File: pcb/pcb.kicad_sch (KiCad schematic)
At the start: 88 parts, among them J1 TRRS, J2 TRRS, SW1 SW_PUSH, SW10 SW_PUSH, SW11 SW_PUSH, SW12 SW_PUSH, SW13 SW_PUSH, SW14 SW_PUSH, SW15 SW_PUSH, SW16 SW_PUSH, SW17 SW_PUSH, SW18 SW_PUSH, SW19 SW_PUSH, SW2 SW_PUSH, SW20 SW_PUSH, SW21 SW_PUSH, SW22 SW_PUSH, SW23 SW_PUSH, SW24 SW_PUSH, SW25 SW_PUSH, SW26 SW_PUSH, SW27 SW_PUSH, SW28 SW_PUSH, SW29 SW_PUSH, SW3 SW_PUSH, SW30 SW_PUSH, SW31 SW_PUSH, SW32 SW_PUSH, SW33 SW_PUSH, SW34 SW_PUSH, SW35 SW_PUSH, SW36 SW_PUSH, SW37 SW_PUSH, SW38 SW_PUSH, SW39 SW_PUSH, SW4 SW_PUSH, SW40 SW_PUSH, SW41 SW_PUSH, SW42 SW_PUSH, SW5 SW_PUSH, SW6 SW_PUSH, SW7 SW_PUSH, SW8 SW_PUSH, SW9 SW_PUSH, U1 rp2040-zero, U2 rp2040-zero

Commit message: 1.1: create garbar files, 2.0: create left pcb
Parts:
- D1, D10, D11, D12, D13, D14, D15, D16, D17, D18, D19, D2, D20, D21, D22, D23, D24, D25, D26, D27, D28, D29, D3, D30, D31, D32, D33, D34, D35, D36, D37, D38, D39, D4, D40, D41, D42, D5, D6, D7, D8, D9: footprint kbd:D3_SMD_v2 -> kbd:D3_TH_SMD_v2
- J1, J2: symbol BrownSugar_KBD:TRRS -> kbd:MJ-4PP-9
- SW1, SW27: footprint kbd:ChocV1_V2_Hotswap_1.5u -> kbd:keyswitch_cherrymx_choc12_hotswap_1.5u
- SW10, SW11, SW12, SW14, SW15, SW16, SW17, SW18, SW2, SW20, SW22, SW23, SW24, SW25, SW26, SW28, SW29, SW3, SW30, SW31, SW32, SW33, SW34, SW35, SW36, SW37, SW38, SW4, SW41, SW5, SW6, SW8, SW9: footprint kbd:ChocV1_V2_Hotswap -> kbd:keyswitch_cherrymx_choc12_hotswap_1u
- SW13, SW19, SW21, SW39, SW40, SW42, SW7: footprint kbd:ChocV1_V2_Hotswap_1.25u -> kbd:keyswitch_cherrymx_choc12_hotswap_1.25u
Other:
- moved on the sheet: U1

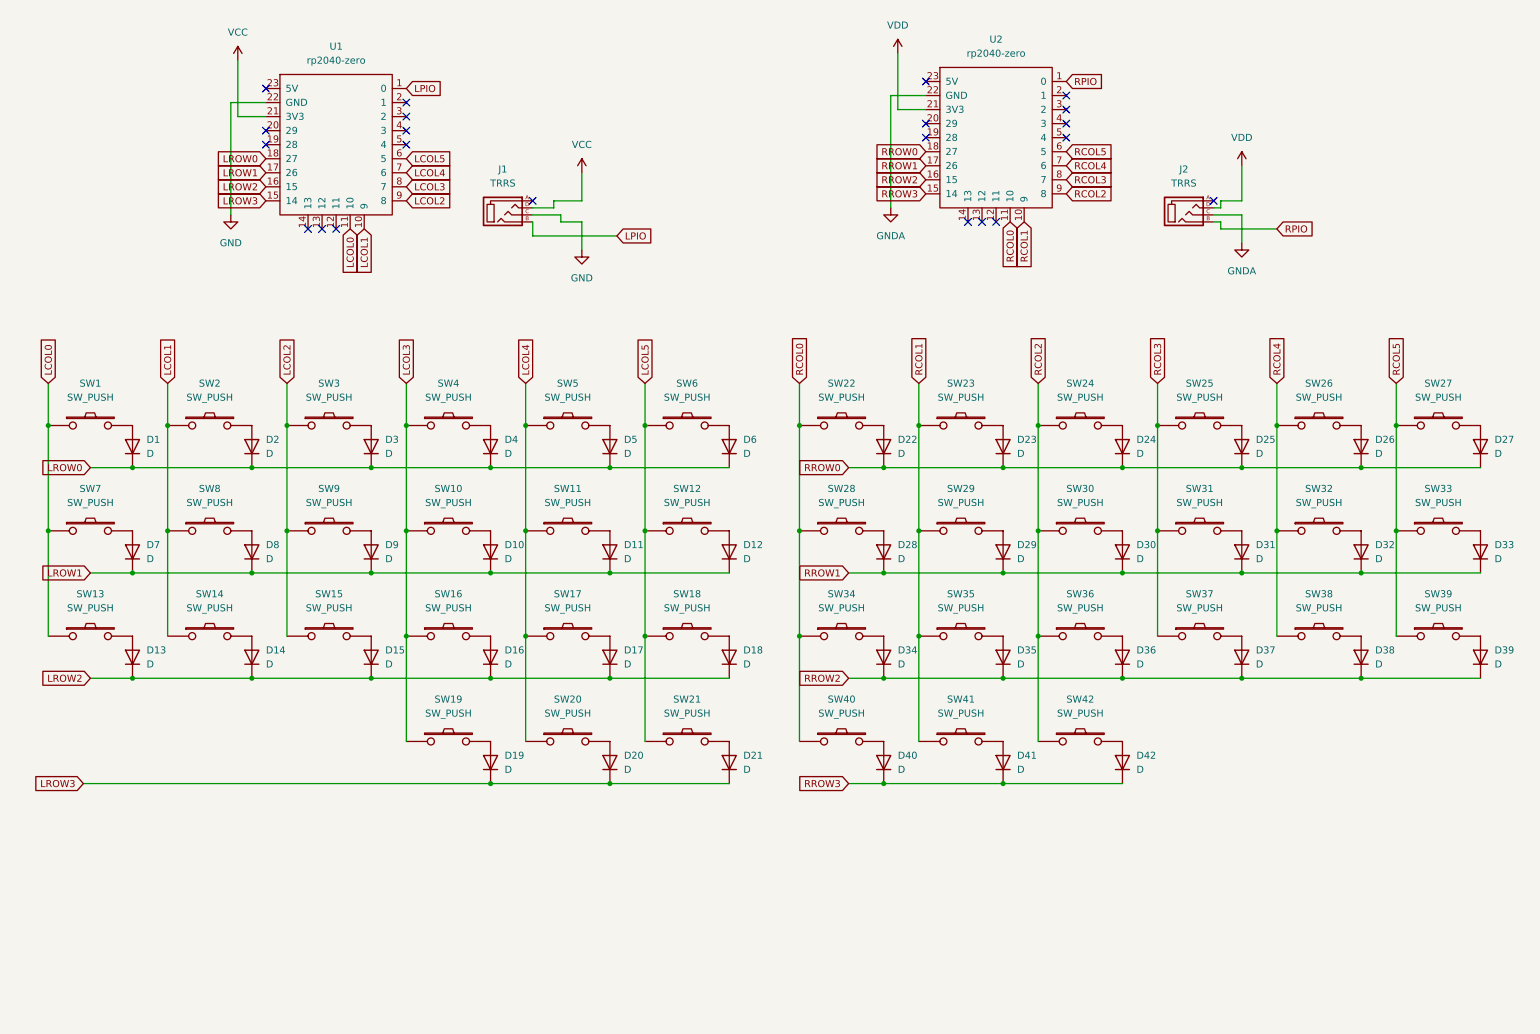
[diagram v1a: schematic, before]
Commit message: refactor: change folder name, old data is no maggie42cs0
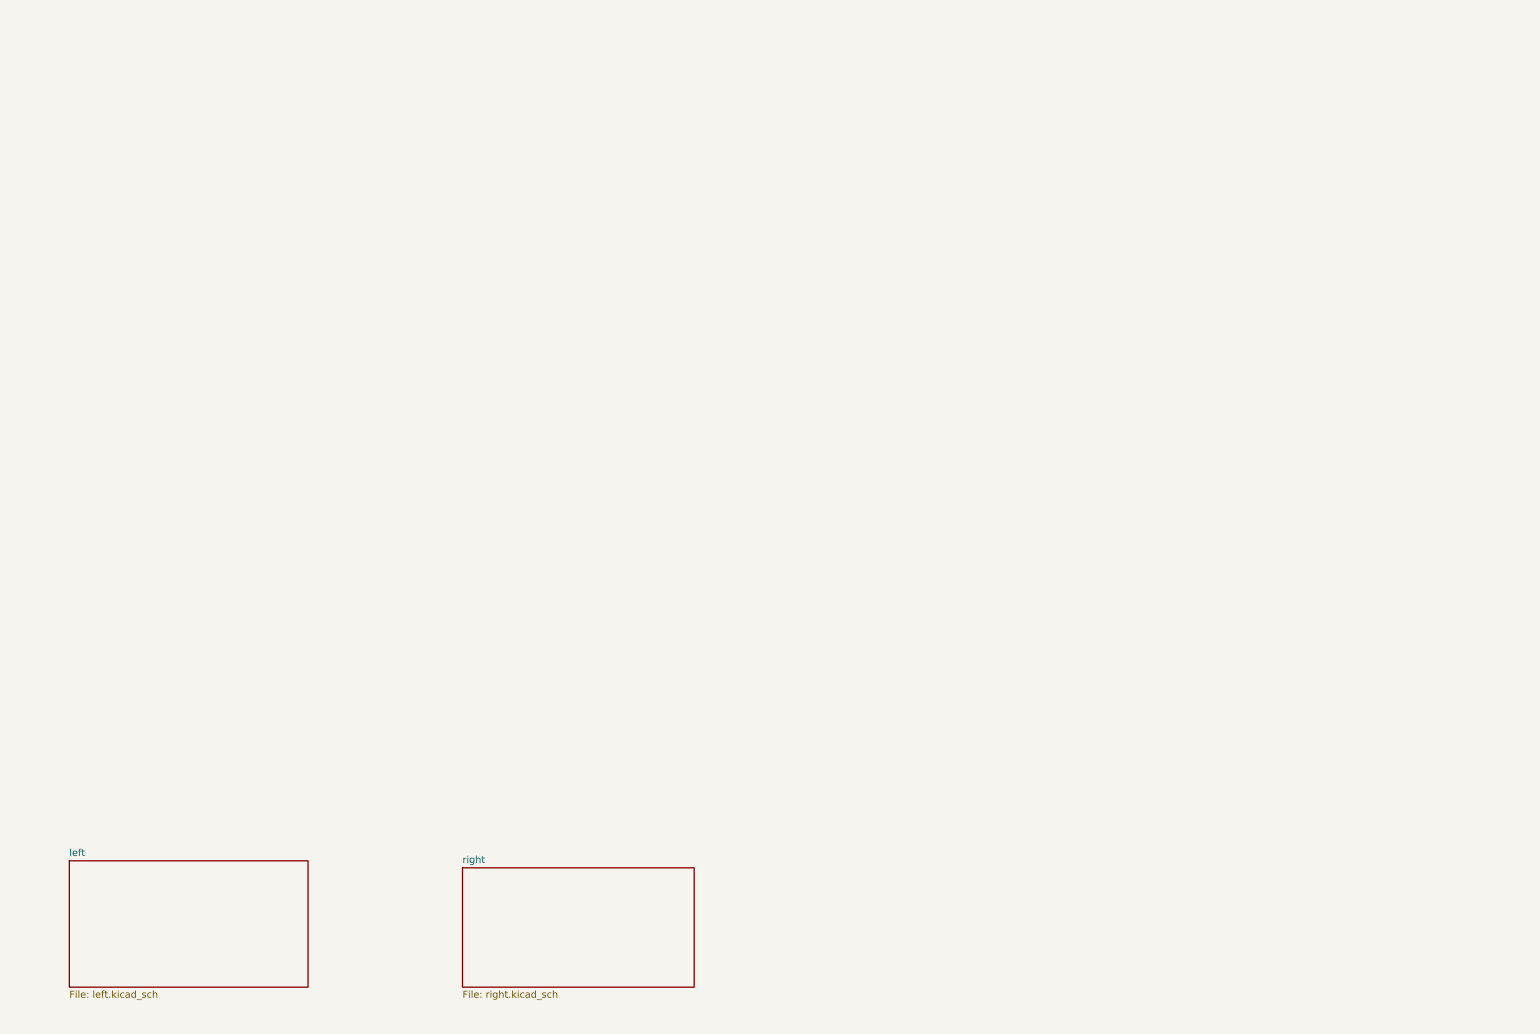
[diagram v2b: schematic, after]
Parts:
- removed D1, D10, D11, D12, D13, D14, D15, D16, D17, D18, D19, D2, D20, D21, D22, D23, D24, D25, D26, D27, D28, D29, D3, D30, D31, D32, D33, D34, D35, D36, D37, D38, D39, D4, D40, D41, D42, D5, D6, D7, D8, D9: D, kbd:D3_TH_SMD_v2, symbol Device:D
- removed J1, J2: TRRS, kbd:MJ-4PP-9_1side, symbol kbd:MJ-4PP-9
- removed SW1, SW27: SW_PUSH, kbd:keyswitch_cherrymx_choc12_hotswap_1.5u, symbol BrownSugar_KBD:SW_PUSH
- removed SW10, SW11, SW12, SW14, SW15, SW16, SW17, SW18, SW2, SW20, SW22, SW23, SW24, SW25, SW26, SW28, SW29, SW3, SW30, SW31, SW32, SW33, SW34, SW35, SW36, SW37, SW38, SW4, SW41, SW5, SW6, SW8, SW9: SW_PUSH, kbd:keyswitch_cherrymx_choc12_hotswap_1u, symbol BrownSugar_KBD:SW_PUSH
- removed SW13, SW19, SW21, SW39, SW40, SW42, SW7: SW_PUSH, kbd:keyswitch_cherrymx_choc12_hotswap_1.25u, symbol BrownSugar_KBD:SW_PUSH
- removed U1, U2: rp2040-zero, mcu:rp2040-zero-tht, symbol mcu:rp2040-zero
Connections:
- no-connect marks 22 -> 0
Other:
- added sheet left (left.kicad_sch)
- added sheet right (right.kicad_sch)
- title: (none) -> maggie42cs

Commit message: wip: layout
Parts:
- added C1, C16, C17, C2: 10u, Capacitor_SMD:C_0402_1005Metric, symbol Device:C_Small
- added C10, C11, C12, C13, C18, C19, C20, C23, C24, C25, C26, C27, C28, C3, C31, C33, C4, C7, C8, C9: 100n, Capacitor_SMD:C_0402_1005Metric, symbol Device:C_Small
- added C14, C15, C29, C30: 30pF, Capacitor_SMD:C_0603_1608Metric, symbol Device:C_Small
- added C21, C22, C32, C34, C5, C6: 2.2uF, Capacitor_SMD:C_0402_1005Metric, symbol Device:C_Small
- added F1, F2: ~, Fuse:Fuse_0603_1608Metric, symbol Device:Polyfuse_Small
- added J1, J4: AudioJack3, kbd:PJ-399B-6A_margin, symbol Connector_Audio:AudioJack3
- added J2, J5: USB_C_Receptacle_USB2.0_16P, Connector_USB:USB_C_Receptacle_HRO_TYPE-C-31-M-12, symbol Connector:USB_C_Receptacle_USB2.0_16P
- added J3, J6: Conn_01x03_Pin, Connector_PinHeader_2.54mm:PinHeader_1x03_P2.54mm_Vertical, symbol Connector:Conn_01x03_Pin
- added R1, R10, R2, R9: 5.1k, Resistor_SMD:R_0402_1005Metric, symbol Device:R_Small
- added R11, R4: 5.6k, Resistor_SMD:R_0603_1608Metric, symbol Device:R_Small
- added R12, R16, R18, R20, R3, R8: 1k, Resistor_SMD:R_0402_1005Metric, symbol Device:R_Small
- added R13, R17, R19, R5: 10k, Resistor_SMD:R_0402_1005Metric, symbol Device:R_Small
- added R14, R15, R6, R7: 27, Resistor_SMD:R_0402_1005Metric, symbol Device:R_Small
- added SD1, SD2: ~, Diode_SMD:D_SOD-123, symbol Device:D_Schottky_Small
- added SMDSW1, SMDSW3: RESET, Button_Switch_SMD:SW_Push_1P1T_XKB_TS-1187A, symbol Switch:SW_Push
- added SMDSW2, SMDSW4: BOOT, Button_Switch_SMD:SW_Push_1P1T_XKB_TS-1187A, symbol Switch:SW_Push
- added STLED1, STLED2: WHITE, LED_SMD:LED_0603_1608Metric, symbol Device:LED_Small
- added U1, U4: NCP1117-3.3_SOT223, Package_TO_SOT_SMD:SOT-223-3_TabPin2, symbol Regulator_Linear:NCP1117-3.3_SOT223
- added U2, U5: RP2040, Package_DFN_QFN:QFN-56-1EP_7x7mm_P0.4mm_EP3.2x3.2mm, symbol MCU_RaspberryPi:RP2040
- added U3, U6: W25Q128JVS, Package_SO:SOIC-8_5.23x5.23mm_P1.27mm, symbol Memory_Flash:W25Q128JVS
- added Y1, Y2: 12MHz, Crystal:Crystal_SMD_3225-4Pin_3.2x2.5mm, symbol Device:Crystal_GND24_Small
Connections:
- new net: R15.2, U5.46 (USB_DM)
- new net: C29.2, U5.20 (XIN), Y2.1
- new net: SMDSW1.2, U2.26 (RUN)
- new net: R7.2, U2.46 (USB_DM)
- new net: C30.2, R16.1, Y2.3
- new net: R20.2, SMDSW4.2
- new net: J2.A5 (CC1), R1.1
- new net: J2.B5 (CC2), R2.1
- new net: C14.2, U2.20 (XIN), Y1.1
- new net: C15.2, R8.1, Y1.3
- new net: J5.A5 (CC1), R9.1
- new net: R3.1, STLED1.2 (A)
- new net: F1.2, R4.1, SD1.2 (A)
- new net: R6.2, U2.47 (USB_DP)
- new net: R16.2, U5.21 (XOUT)
- new net: J6.1 (Pin_1), U5.24 (SWCLK)
- new net: J6.3 (Pin_3), U5.25 (SWD)
- new net: SMDSW3.2, U5.26 (RUN)
- new net: R14.2, U5.47 (USB_DP)
- new net: F2.2, R11.1, SD2.2 (A)
- new net: J3.1 (Pin_1), U2.24 (SWCLK)
- new net: J3.3 (Pin_3), U2.25 (SWD)
- new net: J5.B5 (CC2), R10.1
- new net: R18.2, SMDSW2.2
- new net: R8.2, U2.21 (XOUT)
- new net: R12.1, STLED2.2 (A)
- new net +1V1: C3.1, C4.1, C5.1, U2.23 (DVDD), U2.45 (VREG_VOUT), U2.50 (DVDD)
- new net +3V3: C10.1, C11.1, C12.1, C13.1, C2.1, C31.2, C32.2, C6.1, C7.1, C8.1, C9.1, R17.2, R3.2, U1.2 (VO), U2.1 (IOVDD), U2.10 (IOVDD), U2.22 (IOVDD), U2.33 (IOVDD), U2.42 (IOVDD), U2.43 (ADC_AVDD), U2.44 (VREG_IN), U2.48 (USB_VDD), U2.49 (IOVDD), U3.8 (VCC)
- new net +5V: C1.1, J1.T, SD1.1 (K), U1.3 (VI)
- new net COL0: U2.8 (GPIO6)
- new net COL1: U2.9 (GPIO7)
- new net COL2: U2.11 (GPIO8)
- new net COL3: U2.12 (GPIO9)
- new net COL4: U2.13 (GPIO10)
- new net COL5: U2.14 (GPIO11)
- new net CONN: J1.R, U2.2 (GPIO0)
- new net D+: J2.A6 (D+), J2.B6 (D+), R6.1
- new net D-: J2.A7 (D-), J2.B7 (D-), R7.1
- new net GND: C1.2, C10.2, C11.2, C12.2, C13.2, C14.1, C15.1, C2.2, C3.2, C31.1, C32.1, C4.2, C5.2, C6.2, C7.2, C8.2, C9.2, J1.S, J2.A1 (GND), J2.A12 (GND), J2.B1 (GND), J2.B12 (GND), J2.S1 (SHIELD), J3.2 (Pin_2), R1.2, R13.2, R2.2, R5.2, SMDSW1.1, SMDSW2.1, STLED1.1 (K), U1.1 (GND), U2.19 (TESTEN), U2.57 (GND), U3.4 (GND), Y1.2, Y1.4
- new net QSPI_SCLK: U2.52 (QSPI_SCLK), U3.6 (CLK)
- new net QSPI_SD0: U2.53 (QSPI_SD0), U3.5 (DI(IO0))
- new net QSPI_SD1: U2.55 (QSPI_SD1), U3.2 (DO(IO1))
- new net QSPI_SD2: U2.54 (QSPI_SD2), U3.3 (IO2)
- new net QSPI_SD3: U2.51 (QSPI_SD3), U3.7 (IO3)
- new net QSPI_SS: R17.1, R18.1, U2.56 (QSPI_SS), U3.1 (~{CS})
- new net ROW0: U2.4 (GPIO2)
- new net ROW1: U2.5 (GPIO3)
- new net ROW2: U2.6 (GPIO4)
- new net ROW3: U2.7 (GPIO5)
- new net USB: R4.2, R5.1, U2.3 (GPIO1)
- new net VBUS: F1.1, J2.A4 (VBUS), J2.A9 (VBUS), J2.B4 (VBUS), J2.B9 (VBUS)
- new net VBUSR: F2.1, J5.A4 (VBUS), J5.A9 (VBUS), J5.B4 (VBUS), J5.B9 (VBUS)
- new net r+1V1: C18.1, C19.1, C21.1, U5.23 (DVDD), U5.45 (VREG_VOUT), U5.50 (DVDD)
- new net r+3V3: C17.1, C20.1, C22.1, C23.1, C24.1, C25.1, C26.1, C27.1, C28.1, C33.2, C34.2, R12.2, R19.2, U4.2 (VO), U5.1 (IOVDD), U5.10 (IOVDD), U5.22 (IOVDD), U5.33 (IOVDD), U5.42 (IOVDD), U5.43 (ADC_AVDD), U5.44 (VREG_IN), U5.48 (USB_VDD), U5.49 (IOVDD), U6.8 (VCC)
- new net r+5V: C16.1, J4.T, SD2.1 (K), U4.3 (VI)
- new net rCOL0: U5.8 (GPIO6)
- new net rCOL1: U5.9 (GPIO7)
- new net rCOL2: U5.11 (GPIO8)
- new net rCOL3: U5.12 (GPIO9)
- new net rCOL4: U5.13 (GPIO10)
- new net rCOL5: U5.14 (GPIO11)
- new net rCONN: J4.R, U5.2 (GPIO0)
- new net rD+: J5.A6 (D+), J5.B6 (D+), R14.1
- new net rD-: J5.A7 (D-), J5.B7 (D-), R15.1
- new net rGND: C16.2, C17.2, C18.2, C19.2, C20.2, C21.2, C22.2, C23.2, C24.2, C25.2, C26.2, C27.2, C28.2, C29.1, C30.1, C33.1, C34.1, J4.S, J5.A1 (GND), J5.A12 (GND), J5.B1 (GND), J5.B12 (GND), J5.S1 (SHIELD), J6.2 (Pin_2), R10.2, R9.2, SMDSW3.1, SMDSW4.1, STLED2.1 (K), U4.1 (GND), U5.19 (TESTEN), U5.57 (GND), U6.4 (GND), Y2.2, Y2.4
- new net rQSPI_SCLK: U5.52 (QSPI_SCLK), U6.6 (CLK)
- new net rQSPI_SD0: U5.53 (QSPI_SD0), U6.5 (DI(IO0))
- new net rQSPI_SD1: U5.55 (QSPI_SD1), U6.2 (DO(IO1))
- new net rQSPI_SD2: U5.54 (QSPI_SD2), U6.3 (IO2)
- new net rQSPI_SD3: U5.51 (QSPI_SD3), U6.7 (IO3)
- new net rQSPI_SS: R19.1, R20.1, U5.56 (QSPI_SS), U6.1 (~{CS})
- new net rROW0: U5.4 (GPIO2)
- new net rROW1: U5.5 (GPIO3)
- new net rROW2: U5.6 (GPIO4)
- new net rROW3: U5.7 (GPIO5)
- new net rUSB: R11.2, R13.1, U5.3 (GPIO1)
- no-connect marks 0 -> 40
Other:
- removed sheet left
- removed sheet right
- added sheet key_layout (key_layout.kicad_sch)
- note added: "44pin"
- note added: "45pin"

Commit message: wip
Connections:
- net GND: now also J3.1 (Pin_1); no longer J3.2 (Pin_2), R13.2
- net rGND: now also J6.1 (Pin_1), R13.2; no longer J6.2 (Pin_2)
- net at U5.24 (SWCLK): now also J6.2 (Pin_2); no longer J6.1 (Pin_1)
- net at U2.24 (SWCLK): now also J3.2 (Pin_2); no longer J3.1 (Pin_1)
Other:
- moved on the sheet: J3, J6
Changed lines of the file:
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@@
 	(title_block
 		(title "maggie42cs")
-		(rev "2.0.1")
+		(rev "2.0.2")
 	)
 	(junction
@@
 	(wire
 		(pts
-			(xy 162.56 148.59) (xy 171.45 148.59)
+			(xy 162.56 146.05) (xy 171.45 146.05)
 		)
 		(stroke
@@
 	(wire
 		(pts
+			(xy 24.13 157.48) (xy 33.02 157.48)
+		)
+		(stroke
+			(width 0)
+			(type default)
+		)
+	)
+	(wire
+		(pts
 			(xy 161.29 128.27) (xy 161.29 133.35)
 		)
@@
 	(wire
 		(pts
-			(xy 171.45 146.05) (xy 171.45 148.59)
-		)
-		(stroke
-			(width 0)
-			(type default)
-		)
-	)
-	(wire
-		(pts
 			(xy 162.56 143.51) (xy 171.45 143.51)
 		)
@@
 	(wire
 		(pts
-			(xy 24.13 160.02) (xy 33.02 160.02)
-		)
-		(stroke
-			(width 0)
-			(type default)
-		)
-	)
-	(wire
-		(pts
 			(xy 210.82 59.69) (xy 238.76 59.69)
 		)
@@
 	(wire
 		(pts
-			(xy 33.02 157.48) (xy 33.02 160.02)
-		)
-		(stroke
-			(width 0)
-			(type default)
-		)
-	)
-	(wire
-		(pts
 			(xy 171.45 123.19) (xy 166.37 123.19)
 		)
@@
 	(symbol
 		(lib_id "power:GND")
-		(at 162.56 146.05 90)
+		(at 162.56 140.97 90)
 		(unit 1)
 		(exclude_from_sim no)
@@
 		(fields_autoplaced yes)
 		(property "Reference" "#PWR052"
-			(at 168.91 146.05 0)
+			(at 168.91 140.97 0)
 			(effects
 				(font
@@
 		)
 		(property "Value" "rGND"
-			(at 166.37 146.0499 90)
+			(at 166.37 140.9699 90)
 			(effects
 				(font
@@
 		)
 		(property "Footprint" ""
-			(at 162.56 146.05 0)
+			(at 162.56 140.97 0)
 			(effects
 				(font
@@
 		)
 		(property "Datasheet" ""
-			(at 162.56 146.05 0)
+			(at 162.56 140.97 0)
 			(effects
 				(font
@@
 		)
 		(property "Description" "Power symbol creates a global label with name \"GND\" , ground"
-			(at 162.56 146.05 0)
+			(at 162.56 140.97 0)
 			(effects
 				(font
@@
 			)
 		)
-		(property "Value" "GND"
-			(at 191.77 54.61 0)
+		(property "Value" "rGND"
+			(at 194.31 50.7999 0)
 			(effects
 				(font
 					(size 1.27 1.27)
 				)
+				(justify left)
 			)
 		)
@@
 	(symbol
 		(lib_id "Connector:Conn_01x03_Pin")
-		(at 19.05 157.48 0)
+		(at 19.05 154.94 0)
 		(unit 1)
 		(exclude_from_sim no)
@@
 		(dnp no)
 		(property "Reference" "J3"
-			(at 19.685 149.86 0)
+			(at 19.685 147.32 0)
 			(effects
 				(font
@@
 		)
 		(property "Value" "Conn_01x03_Pin"
-			(at 23.622 151.892 0)
+			(at 23.622 149.352 0)
 			(effects
 				(font
@@
 		)
 		(property "Footprint" "Connector_PinHeader_2.54mm:PinHeader_1x03_P2.54mm_Vertical"
-			(at 19.05 157.48 0)
+			(at 19.05 154.94 0)
 			(effects
 				(font
@@
 		)
 		(property "Datasheet" "~"
-			(at 19.05 157.48 0)
+			(at 19.05 154.94 0)
 			(effects
 				(font
@@
 		)
 		(property "Description" "Generic connector, single row, 01x03, script generated"
-			(at 19.05 157.48 0)
+			(at 19.05 154.94 0)
 			(effects
 				(font
@@
 	(symbol
 		(lib_id "power:GND")
-		(at 24.13 157.48 90)
+		(at 24.13 152.4 90)
 		(unit 1)
 		(exclude_from_sim no)
@@
 		(fields_autoplaced yes)
 		(property "Reference" "#PWR054"
-			(at 30.48 157.48 0)
+			(at 30.48 152.4 0)
 			(effects
 				(font
@@
 		)
 		(property "Value" "GND"
-			(at 27.94 157.4799 90)
+			(at 27.94 152.3999 90)
 			(effects
 				(font
@@
 		)
 		(property "Footprint" ""
-			(at 24.13 157.48 0)
+			(at 24.13 152.4 0)
 			(effects
 				(font
@@
 		)
 		(property "Datasheet" ""
-			(at 24.13 157.48 0)
+			(at 24.13 152.4 0)
 			(effects
 				(font
@@
 		)
 		(property "Description" "Power symbol creates a global label with name \"GND\" , ground"
-			(at 24.13 157.48 0)
+			(at 24.13 152.4 0)
 			(effects
 				(font
@@
 	(symbol
 		(lib_id "Connector:Conn_01x03_Pin")
-		(at 157.48 146.05 0)
+		(at 157.48 143.51 0)
 		(unit 1)
 		(exclude_from_sim no)
@@
 		(dnp no)
 		(property "Reference" "J6"
-			(at 158.115 138.43 0)
+			(at 158.115 135.89 0)
 			(effects
 				(font
@@
 		)
 		(property "Value" "Conn_01x03_Pin"
-			(at 163.83 140.716 0)
+			(at 163.83 138.176 0)
 			(effects
 				(font
@@
 		)
 		(property "Footprint" "Connector_PinHeader_2.54mm:PinHeader_1x03_P2.54mm_Vertical"
-			(at 157.48 146.05 0)
+			(at 157.48 143.51 0)
 			(effects
 				(font
@@
 		)
 		(property "Datasheet" "~"
-			(at 157.48 146.05 0)
+			(at 157.48 143.51 0)
 			(effects
 				(font
@@
 		)
 		(property "Description" "Generic connector, single row, 01x03, script generated"
-			(at 157.48 146.05 0)
+			(at 157.48 143.51 0)
 			(effects
 				(font

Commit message: add: pcb and plate garber files
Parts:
- SMDSW3, SMDSW4: LCSC C455280 -> C318884
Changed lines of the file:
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@@
 			)
 		)
-		(property "LCSC" "C455280"
+		(property "LCSC" "C318884"
 			(at 236.22 139.7 0)
 			(effects
@@
 			)
 		)
-		(property "LCSC" "C455280"
+		(property "LCSC" "C318884"
 			(at 166.37 77.47 0)
 			(effects
